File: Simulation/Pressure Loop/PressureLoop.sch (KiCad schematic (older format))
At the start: 87 parts, among them Q10 BCY58, Q11 BCY58, Q12 BCY58, Q3 BCY58, Q4 BCY58, Q5 BCY58, Q6 BCY58, Q7 BCY58, Q8 BCY58, Q9 BCY58

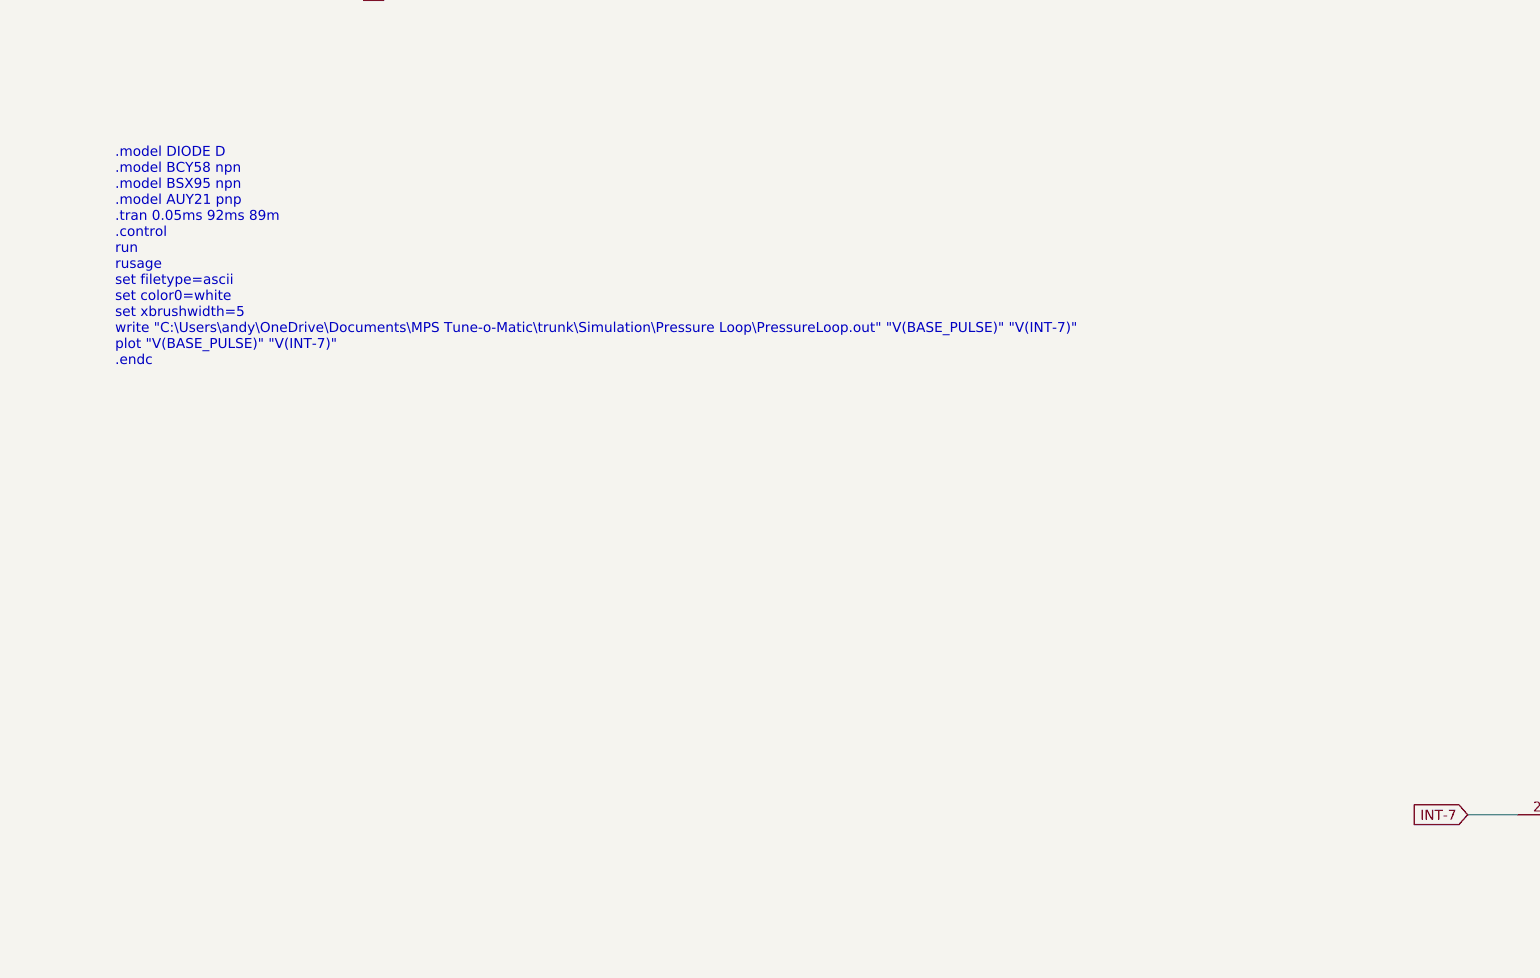
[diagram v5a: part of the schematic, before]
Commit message: Added more simulation scenarios.
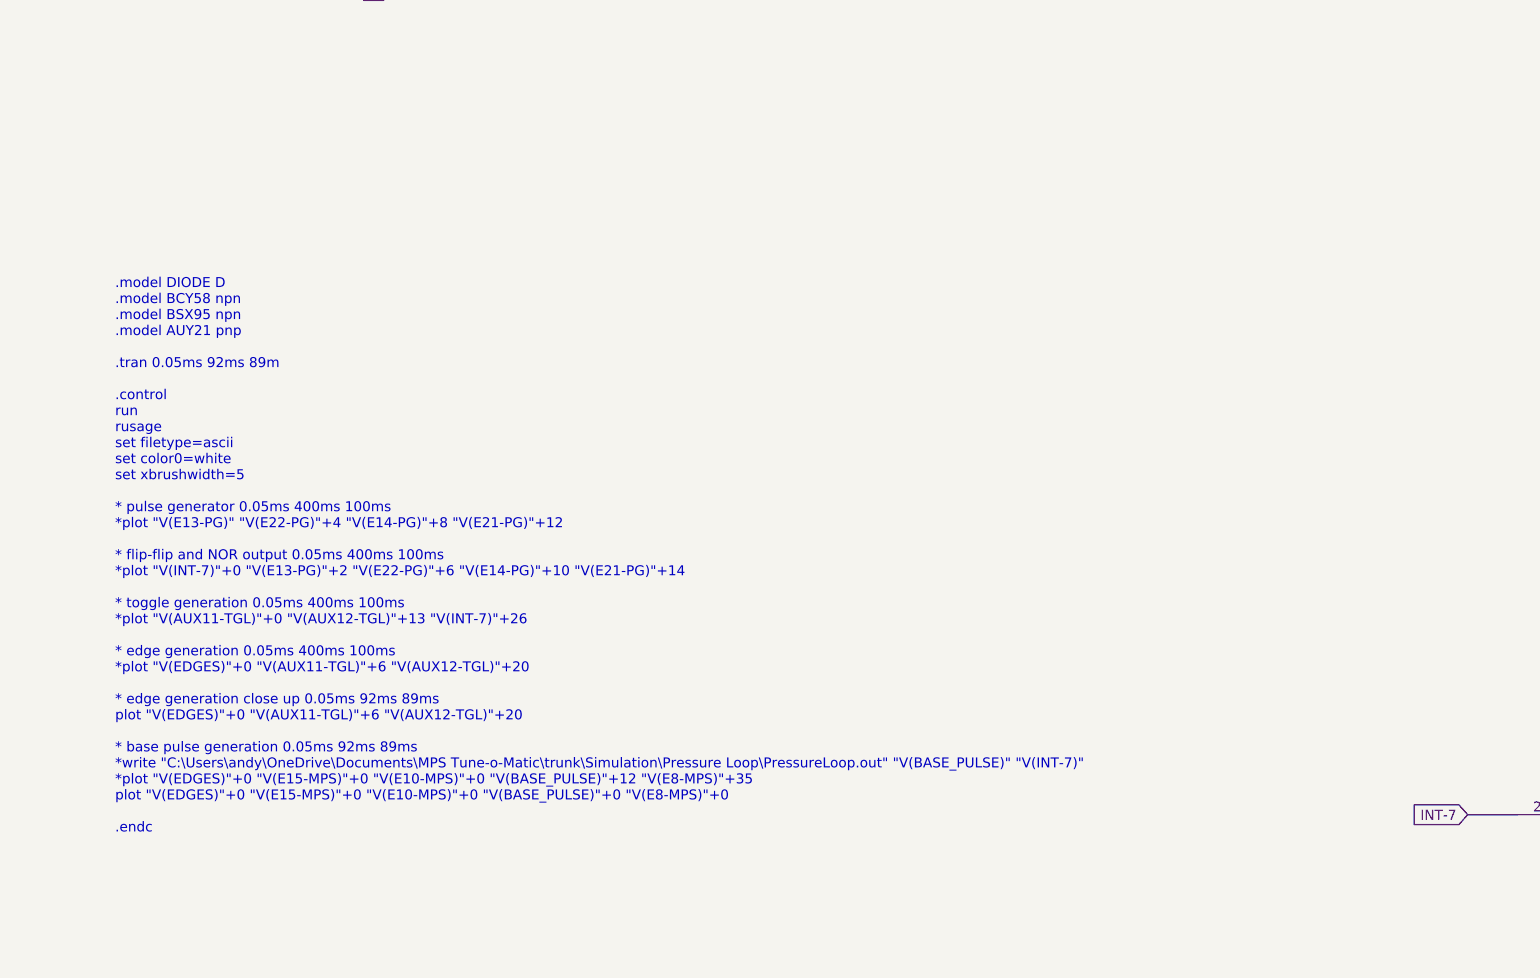
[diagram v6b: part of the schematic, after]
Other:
- note added: ".model DIODE D\n.model BCY58 npn\n.model BSX95 npn\n.model AUY21 pnp\n\n.tran 0.05ms 92ms 89m\n\n.control\nrun\nrusage\nset filetype=ascii\nset color0=white\nset xbrushwidth=5\n\n* pulse generator 0.05ms 400ms 100ms\n*plot "V(E13-PG)" "V(E22-PG)"+4 "V(E14-PG)"+8 "V(E21-PG)"+12\n\n* flip-flip and NOR output 0.05ms 400ms 100ms\n*plot "V(INT-7)"+0 "V(E13-PG)"+2 "V(E22-PG)"+6 "V(E14-PG)"+10 "V(E21-PG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"
- note removed: ".model DIODE D\n.model BCY58 npn\n.model BSX95 npn\n.model AUY21 pnp\n.tran 0.05ms 92ms 89m\n.control\nrun\nrusage\nset filetype=ascii\nset color0=white\nset xbrushwidth=5\nwrite "C:\Users\andy\OneDrive\Documents\MPS Tune-o-Matic\trunk\Simulation\Pressure Loop\PressureLoop.out" "V(BASE_PULSE)" "V(INT-7)"\nplot "V(BASE_PULSE)" "V(INT-7)"\n.endc\n"
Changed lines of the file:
@@
 Wire Wire Line
 	13550 7450 17300 7450
-Text Notes 1350 6950 0    50   ~ 0
-.model DIODE D\n.model BCY58 npn\n.model BSX95 npn\n.model AUY21 pnp\n.tran 0.05ms 92ms 89m\n.control\nrun\nrusage\nset filetype=ascii\nset color0=white\nset xbrushwidth=5\nwrite "C:\Users\andy\OneDrive\Documents\MPS Tune-o-Matic\trunk\Simulation\Pressure Loop\PressureLoop.out" "V(BASE_PULSE)" "V(INT-7)"\nplot "V(BASE_PULSE)" "V(INT-7)"\n.endc\n
 Wire Wire Line
 	6150 12850 6150 12750
@@
 Text Notes 850  4700 0    50   ~ 0
 Lower voltage = richer
+Text Notes 1350 9300 0    50   ~ 0
+.model DIODE D\n.model BCY58 npn\n.model BSX95 npn\n.model AUY21 pnp\n\n.tran 0.05ms 92ms 89m\n\n.control\nrun\nrusage\nset filetype=ascii\nset color0=white\nset xbrushwidth=5\n\n* pulse generator 0.05ms 400ms 100ms\n*plot "V(E13-PG)" "V(E22-PG)"+4 "V(E14-PG)"+8 "V(E21-PG)"+12\n\n* flip-flip and NOR output 0.05ms 400ms 100ms\n*plot "V(INT-7)"+0 "V(E13-PG)"+2 "V(E22-PG)"+6 "V(E14-PG)"+10 "V(E21-PG)"+14\n\n* toggle generation 0.05ms 400ms 100ms\n*plot "V(AUX11-TGL)"+0 "V(AUX12-TGL)"+13 "V(INT-7)"+26\n\n* edge generation 0.05ms 400ms 100ms\n*plot "V(EDGES)"+0 "V(AUX11-TGL)"+6 "V(AUX12-TGL)"+20\n\n* edge generation close up 0.05ms 92ms 89ms\nplot "V(EDGES)"+0 "V(AUX11-TGL)"+6 "V(AUX12-TGL)"+20\n\n* base pulse generation 0.05ms 92ms 89ms\n*write "C:\Users\andy\OneDrive\Documents\MPS Tune-o-Matic\trunk\Simulation\Pressure Loop\PressureLoop.out" "V(BASE_PULSE)" "V(INT-7)"\n*plot "V(EDGES)"+0 "V(E15-MPS)"+0 "V(E10-MPS)"+0 "V(BASE_PULSE)"+12 "V(E8-MPS)"+35\nplot "V(EDGES)"+0 "V(E15-MPS)"+0 "V(E10-MPS)"+0 "V(BASE_PULSE)"+0 "V(E8-MPS)"+0\n\n.endc\n
 $EndSCHEMATC

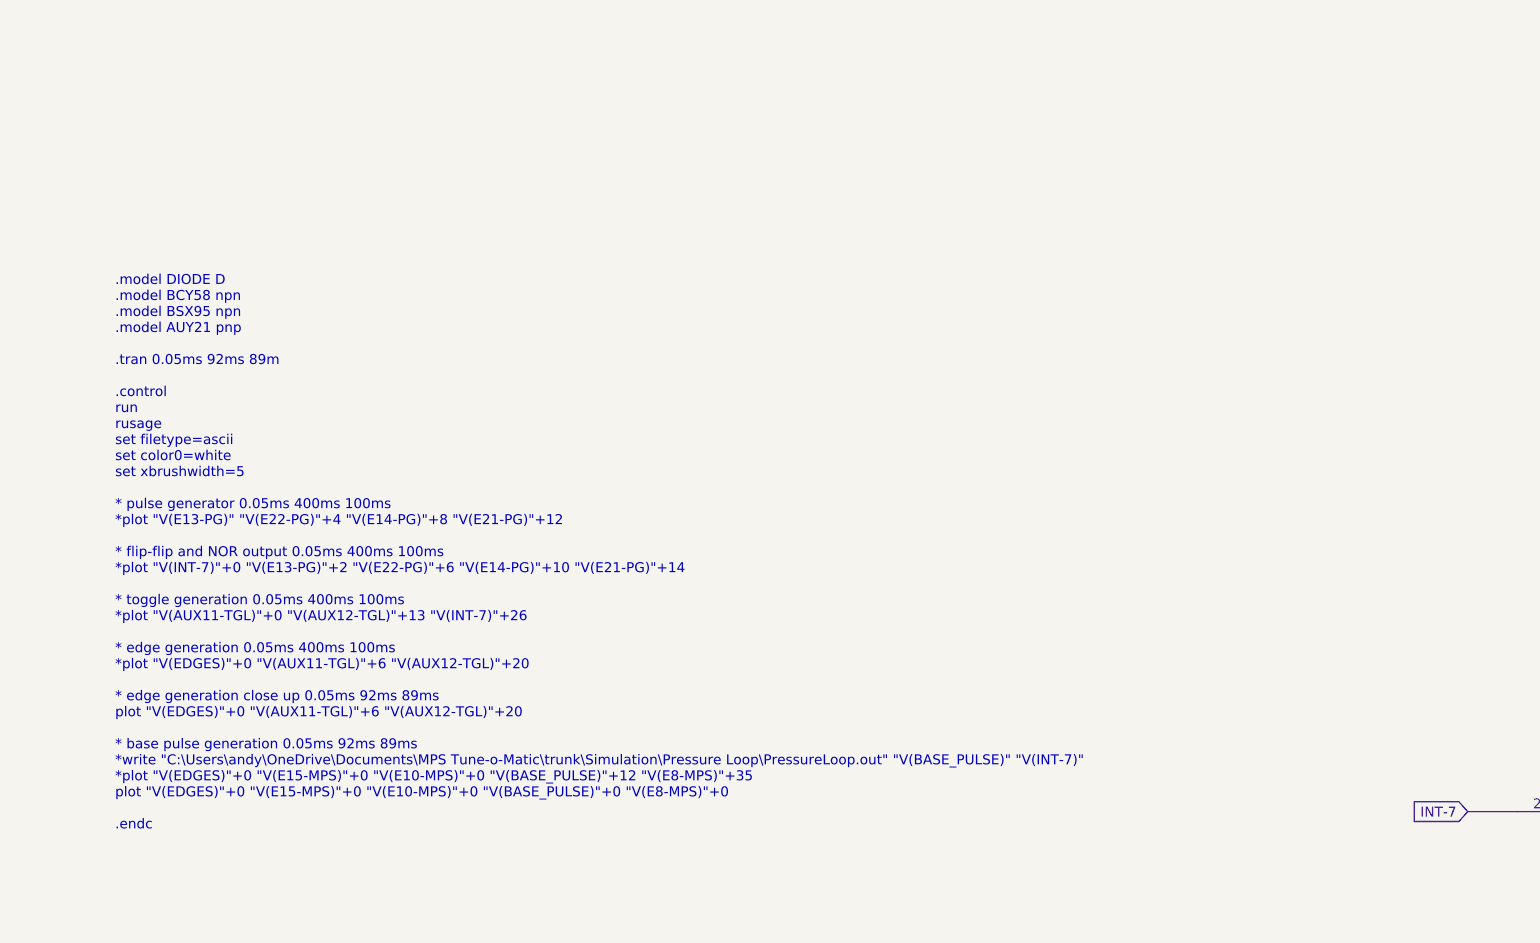
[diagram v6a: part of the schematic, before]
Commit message: Pressure loop simulation now outputs dwell in degrees.
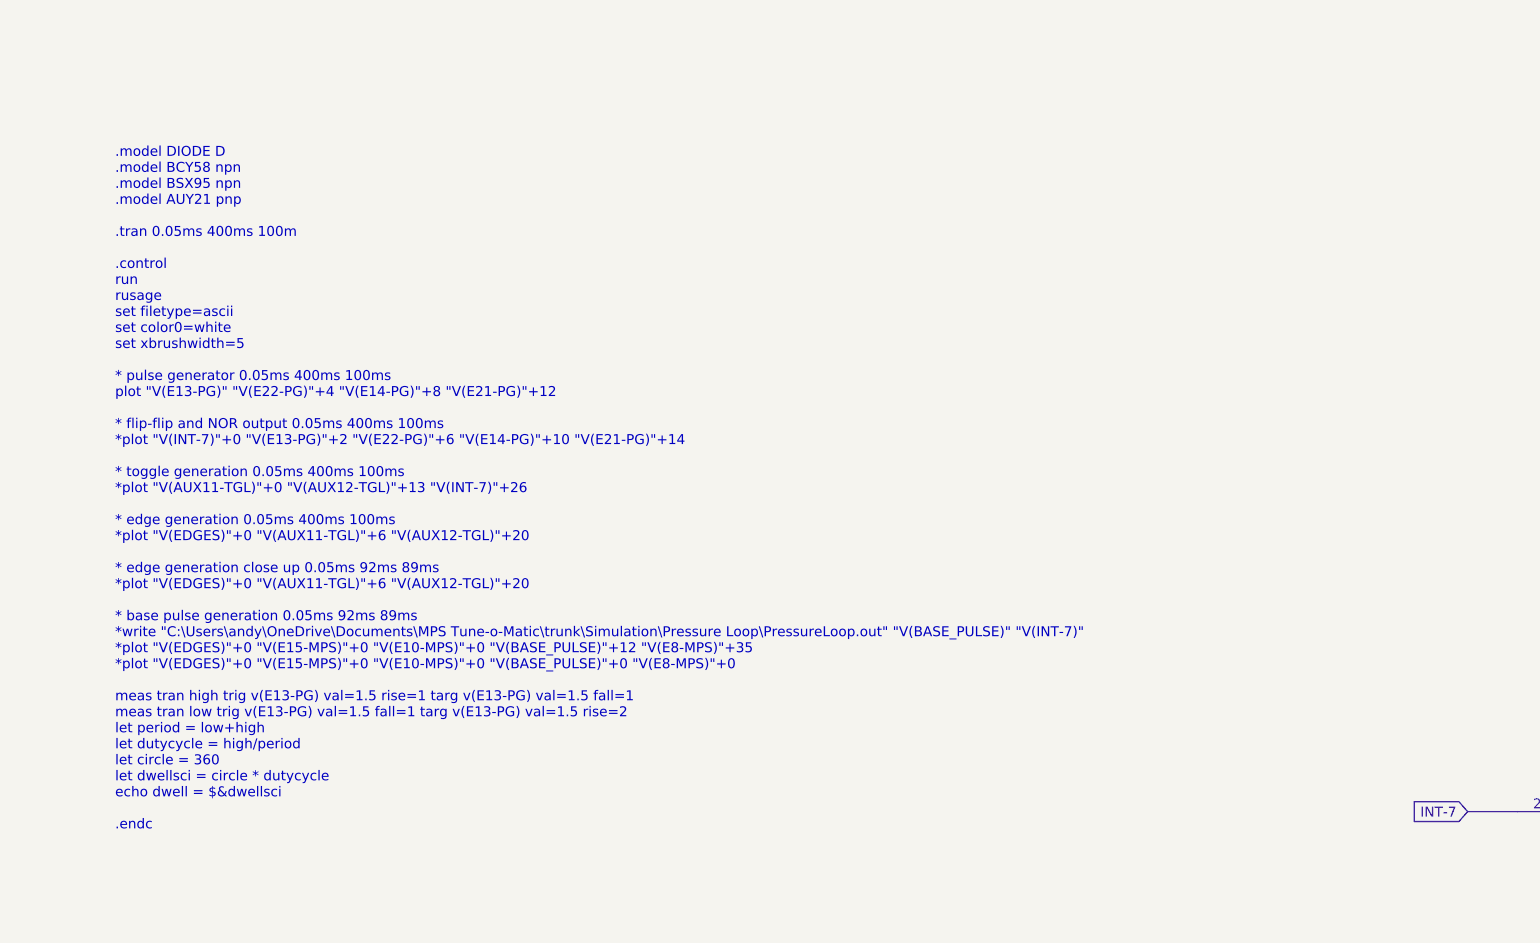
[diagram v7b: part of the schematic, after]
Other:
- note added: ".model DIODE D\n.model BCY58 npn\n.model BSX95 npn\n.model AUY21 pnp\n\n.tran 0.05ms 400ms 100m\n\n.control\nrun\nrusage\nset filetype=ascii\nset color0=white\nset xbrushwidth=5\n\n* pulse generator 0.05ms 400ms 100ms\nplot "V(E13-PG)" "V(E22-PG)"+4 "V(E14-PG)"+8 "V(E21-PG)"+12\n\n* flip-flip and NOR output 0.05ms 400ms 100ms\n*plot "V(INT-7)"+0 "V(E13-PG)"+2 "V(E22-PG)"+6 "V(E14-PG)"+10 "V(E21-P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"
- note removed: ".model DIODE D\n.model BCY58 npn\n.model BSX95 npn\n.model AUY21 pnp\n\n.tran 0.05ms 92ms 89m\n\n.control\nrun\nrusage\nset filetype=ascii\nset color0=white\nset xbrushwidth=5\n\n* pulse generator 0.05ms 400ms 100ms\n*plot "V(E13-PG)" "V(E22-PG)"+4 "V(E14-PG)"+8 "V(E21-PG)"+12\n\n* flip-flip and NOR output 0.05ms 400ms 100ms\n*plot "V(INT-7)"+0 "V(E13-PG)"+2 "V(E22-PG)"+6 "V(E14-PG)"+10 "V(E21-PG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"
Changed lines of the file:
@@
 Lower voltage = richer
 Text Notes 1350 9300 0    50   ~ 0
-.model DIODE D\n.model BCY58 npn\n.model BSX95 npn\n.model AUY21 pnp\n\n.tran 0.05ms 92ms 89m\n\n.control\nrun\nrusage\nset filetype=ascii\nset color0=white\nset xbrushwidth=5\n\n* pulse generator 0.05ms 400ms 100ms\n*plot "V(E13-PG)" "V(E22-PG)"+4 "V(E14-PG)"+8 "V(E21-PG)"+12\n\n* flip-flip and NOR output 0.05ms 400ms 100ms\n*plot "V(INT-7)"+0 "V(E13-PG)"+2 "V(E22-PG)"+6 "V(E14-PG)"+10 "V(E21-PG)"+14\n\n* toggle generation 0.05ms 400ms 100ms\n*plot "V(AUX11-TGL)"+0 "V(AUX12-TGL)"+13 "V(INT-7)"+26\n\n* edge generation 0.05ms 400ms 100ms\n*plot "V(EDGES)"+0 "V(AUX11-TGL)"+6 "V(AUX12-TGL)"+20\n\n* edge generation close up 0.05ms 92ms 89ms\nplot "V(EDGES)"+0 "V(AUX11-TGL)"+6 "V(AUX12-TGL)"+20\n\n* base pulse generation 0.05ms 92ms 89ms\n*write "C:\Users\andy\OneDrive\Documents\MPS Tune-o-Matic\trunk\Simulation\Pressure Loop\PressureLoop.out" "V(BASE_PULSE)" "V(INT-7)"\n*plot "V(EDGES)"+0 "V(E15-MPS)"+0 "V(E10-MPS)"+0 "V(BASE_PULSE)"+12 "V(E8-MPS)"+35\nplot "V(EDGES)"+0 "V(E15-MPS)"+0 "V(E10-MPS)"+0 "V(BASE_PULSE)"+0 "V(E8-MPS)"+0\n\n.endc\n
+.model DIODE D\n.model BCY58 npn\n.model BSX95 npn\n.model AUY21 pnp\n\n.tran 0.05ms 400ms 100m\n\n.control\nrun\nrusage\nset filetype=ascii\nset color0=white\nset xbrushwidth=5\n\n* pulse generator 0.05ms 400ms 100ms\nplot "V(E13-PG)" "V(E22-PG)"+4 "V(E14-PG)"+8 "V(E21-PG)"+12\n\n* flip-flip and NOR output 0.05ms 400ms 100ms\n*plot "V(INT-7)"+0 "V(E13-PG)"+2 "V(E22-PG)"+6 "V(E14-PG)"+10 "V(E21-PG)"+14\n\n* toggle generation 0.05ms 400ms 100ms\n*plot "V(AUX11-TGL)"+0 "V(AUX12-TGL)"+13 "V(INT-7)"+26\n\n* edge generation 0.05ms 400ms 100ms\n*plot "V(EDGES)"+0 "V(AUX11-TGL)"+6 "V(AUX12-TGL)"+20\n\n* edge generation close up 0.05ms 92ms 89ms\n*plot "V(EDGES)"+0 "V(AUX11-TGL)"+6 "V(AUX12-TGL)"+20\n\n* base pulse generation 0.05ms 92ms 89ms\n*write "C:\Users\andy\OneDrive\Documents\MPS Tune-o-Matic\trunk\Simulation\Pressure Loop\PressureLoop.out" "V(BASE_PULSE)" "V(INT-7)"\n*plot "V(EDGES)"+0 "V(E15-MPS)"+0 "V(E10-MPS)"+0 "V(BASE_PULSE)"+12 "V(E8-MPS)"+35\n*plot "V(EDGES)"+0 "V(E15-MPS)"+0 "V(E10-MPS)"+0 "V(BASE_PULSE)"+0 "V(E8-MPS)"+0\n\nmeas tran high trig v(E13-PG) val=1.5 rise=1 targ v(E13-PG) val=1.5 fall=1\nmeas tran low trig v(E13-PG) val=1.5 fall=1 targ v(E13-PG) val=1.5 rise=2\nlet period = low+high\nlet dutycycle = high/period\nlet circle = 360\nlet dwellsci = circle * dutycycle\necho dwell = $&dwellsci\n\n.endc\n
 $EndSCHEMATC
